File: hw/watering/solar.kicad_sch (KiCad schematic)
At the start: 23 parts, among them U2 DRV8220DSG, U5 STI3508

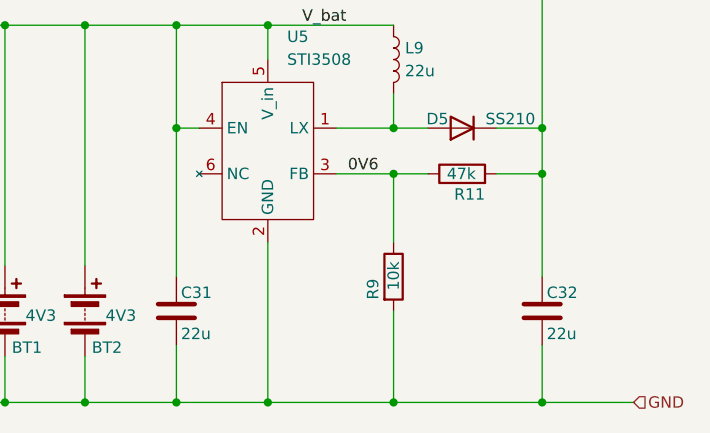
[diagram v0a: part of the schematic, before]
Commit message: - improved voltage boost on battery power - some issues with rtc clock - some issues with pwm that result in brownout
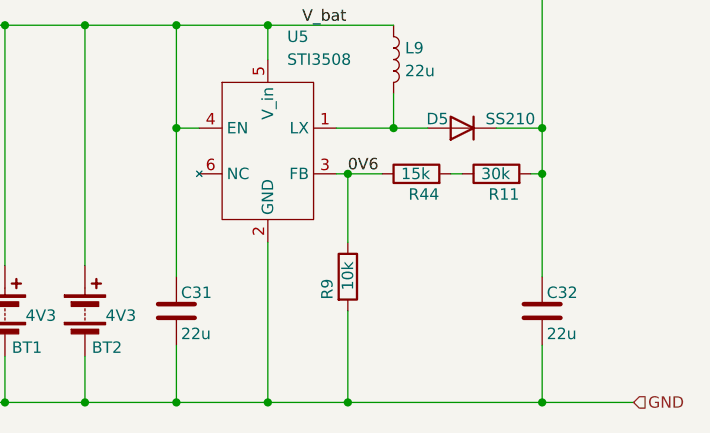
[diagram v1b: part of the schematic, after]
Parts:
- added R44: 15k, Resistor_SMD:R_0603_1608Metric, symbol Device:R
- R11: value 47k -> 30k
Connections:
- net 0V6: now also R44.1; no longer R11.1
- new net: R11.1, R44.2
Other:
- moved on the sheet: R11, R9
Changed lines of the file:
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@@
 	)
 	(junction
+		(at 389.89 220.98)
+		(diameter 0)
+		(color 0 0 0 0)
+	)
+	(junction
 		(at 389.89 246.38)
 		(diameter 0)
@@
 	)
 	(junction
-		(at 389.89 220.98)
-		(diameter 0)
-		(color 0 0 0 0)
-	)
-	(junction
 		(at 389.89 22.86)
 		(diameter 0)
@@
 	)
 	(junction
-		(at 373.38 246.38)
+		(at 368.3 246.38)
 		(diameter 0)
 		(color 0 0 0 0)
@@
 	)
 	(junction
-		(at 373.38 220.98)
-		(diameter 0)
-		(color 0 0 0 0)
-	)
-	(junction
 		(at 271.78 246.38)
 		(diameter 0)
@@
 	)
 	(junction
+		(at 368.3 220.98)
+		(diameter 0)
+		(color 0 0 0 0)
+	)
+	(junction
 		(at 349.25 204.47)
 		(diameter 0)
@@
 	(wire
 		(pts
-			(xy 349.25 246.38) (xy 373.38 246.38)
-		)
-		(stroke
-			(width 0)
-			(type default)
-		)
-	)
-	(wire
-		(pts
-			(xy 373.38 246.38) (xy 400.05 246.38)
+			(xy 349.25 246.38) (xy 368.3 246.38)
 		)
 		(stroke
@@
 	(wire
 		(pts
-			(xy 373.38 220.98) (xy 377.19 220.98)
+			(xy 77.47 227.33) (xy 77.47 217.17)
 		)
 		(stroke
@@
 	(wire
 		(pts
-			(xy 77.47 227.33) (xy 77.47 217.17)
+			(xy 86.36 223.52) (xy 86.36 217.17)
 		)
 		(stroke
@@
 	(wire
 		(pts
-			(xy 86.36 223.52) (xy 86.36 217.17)
+			(xy 236.22 208.28) (xy 252.73 208.28)
 		)
 		(stroke
@@
 	(wire
 		(pts
-			(xy 236.22 208.28) (xy 252.73 208.28)
+			(xy 309.88 246.38) (xy 313.69 246.38)
 		)
 		(stroke
@@
 	(wire
 		(pts
-			(xy 309.88 246.38) (xy 313.69 246.38)
+			(xy 388.62 220.98) (xy 389.89 220.98)
+		)
+		(stroke
+			(width 0)
+			(type default)
+		)
+	)
+	(wire
+		(pts
+			(xy 368.3 220.98) (xy 372.11 220.98)
 		)
 		(stroke
@@
 	(wire
 		(pts
-			(xy 367.03 220.98) (xy 373.38 220.98)
+			(xy 367.03 220.98) (xy 368.3 220.98)
 		)
 		(stroke
@@
 	(wire
 		(pts
-			(xy 373.38 220.98) (xy 373.38 228.6)
+			(xy 368.3 220.98) (xy 368.3 228.6)
 		)
 		(stroke
@@
 	(wire
 		(pts
-			(xy 373.38 236.22) (xy 373.38 246.38)
+			(xy 368.3 236.22) (xy 368.3 246.38)
 		)
 		(stroke
@@
 	(wire
 		(pts
-			(xy 384.81 220.98) (xy 389.89 220.98)
-		)
-		(stroke
-			(width 0)
-			(type default)
-		)
-	)
-	(wire
-		(pts
 			(xy 349.25 204.47) (xy 359.41 204.47)
 		)
@@
 	(wire
 		(pts
+			(xy 379.73 220.98) (xy 381 220.98)
+		)
+		(stroke
+			(width 0)
+			(type default)
+		)
+	)
+	(wire
+		(pts
 			(xy 86.36 242.57) (xy 86.36 246.38)
 		)
@@
 	(wire
 		(pts
+			(xy 368.3 246.38) (xy 400.05 246.38)
+		)
+		(stroke
+			(width 0)
+			(type default)
+		)
+	)
+	(wire
+		(pts
 			(xy 330.2 204.47) (xy 330.2 231.14)
 		)
@@
 	(symbol
 		(lib_id "Device:R")
-		(at 373.38 232.41 0)
+		(at 368.3 232.41 0)
 		(unit 1)
 		(body_style 1)
@@
 		(dnp no)
 		(property "Reference" "R9"
-			(at 371.094 234.95 90)
+			(at 366.014 234.95 90)
 			(show_name no)
 			(do_not_autoplace no)
@@
 		)
 		(property "Value" "10k"
-			(at 373.38 233.934 90)
+			(at 368.3 233.934 90)
 			(show_name no)
 			(do_not_autoplace no)
@@
 		)
 		(property "Footprint" "Resistor_SMD:R_0603_1608Metric"
-			(at 371.602 232.41 90)
+			(at 366.522 232.41 90)
 			(hide yes)
 			(show_name no)
@@
 		)
 		(property "Datasheet" "https://jlc-prod-smt.oss-eu-central-1.aliyuncs.com/smtDataManualFile/8579706381316128768-C25804.pdf?response-content-disposition=attachment%3B%20filename%3DC25804.pdf%3B%20filename%2A%3DUTF-8%27%27C25804.pdf&x-oss-date=20260604T182440Z&x-oss-expires=1800&x-oss-security-token=CAISgAN1q6Ft5B2yfSjIr5nhDvTiu55L8aayRHLFsEERZtthpKj%2B0Dz2IHhMdHJsAOodtv0%2FmmhT6PkclqRLcbhpcmfjV%2BZHzLB8qeRniENA4J7b16cNrbH4M4H6aXeirtuwDsz9SNTCALjPD3nPii50x5bjaDymRCbLGJaViJlhHLN1Ow6jdmhpCctxLAlvo9NgFxm3D%2Fu2NQPwiWf9FVdhvhEG6Vly8qOi2MaRmFy8yFTx0b0SvJ%2BjYMrmPctoN9JnSdC5mfdzau3a1TJ84gRD0a5wkaVA1zbDs5bfISEIuUzebreLqY03dV4mOvdqIcMe8qigz88fk%2FfIioH6xyxKOexoSCnFTOiiupCcQLPyao9jLu6iayqViY7QaIOTqQohZmkAMwVOasAsI3Ngh4zF97Qt0cVNkXO9gWfLI8DtuMleWhri1Udu3tHD0eS19jklBdzSlusJRAJJUVBflCeKEaRNSAd3WGhEfM2%2BBt4QT30w5N2u00S8OSMIOONBvqKWD5sagAGpldF62iBeHzrNV%2BHnUyjaA64BCjacRbVbSjmxSgiuNX1d%2FbCnqQV25prdqNhtDbAKCoRnNQDFNxmhLIIUUcffM9eG3oRc44RNhyi7hADN6z1ILjt6TEoRuXkDAYH1u8iyrE2YQDMkq7F3Cke8dxQ44PYZqWefci6GHDzQ1pzPpiAA&x-oss-signature-version=OSS4-HMAC-SHA256&x-oss-credential=STS.NZTENVVAjFdYFTtTADjTMKmU2%2F20260604%2Feu-central-1%2Foss%2Faliyun_v4_request&x-oss-signature=78c2b620008555fdaf271c3d0b7682edd0aca7d23428d31f63338848e1713cab"
-			(at 373.38 232.41 0)
+			(at 368.3 232.41 0)
 			(hide yes)
 			(show_name no)
@@
 		)
 		(property "Description" "C25804"
-			(at 373.38 232.41 0)
+			(at 368.3 232.41 0)
 			(hide yes)
 			(show_name no)
@@
 	)
 	(symbol
+		(lib_id "Device:R")
+		(at 375.92 220.98 90)
+		(unit 1)
+		(body_style 1)
+		(exclude_from_sim no)
+		(in_bom yes)
+		(on_board yes)
+		(in_pos_files yes)
+		(dnp no)
+		(property "Reference" "R44"
+			(at 378.46 223.266 90)
+			(show_name no)
+			(do_not_autoplace no)
+			(effects
+				(font
+					(size 1.27 1.27)
+				)
+				(justify left)
+			)
+		)
+		(property "Value" "15k"
+			(at 377.444 220.98 90)
+			(show_name no)
+			(do_not_autoplace no)
+			(effects
+				(font
+					(size 1.27 1.27)
+				)
+				(justify left)
+			)
+		)
+		(property "Footprint" "Resistor_SMD:R_0603_1608Metric"
+			(at 375.92 222.758 90)
+			(hide yes)
+			(show_name no)
+			(do_not_autoplace no)
+			(effects
+				(font
+					(size 1.27 1.27)
+				)
+			)
+		)
+		(property "Datasheet" "https://jlc-prod-smt.oss-eu-central-1.aliyuncs.com/smtDataManualFile/8579706364622934016-C25819.pdf?response-content-disposition=attachment%3B%20filename%3DC25819.pdf%3B%20filename%2A%3DUTF-8%27%27C25819.pdf&x-oss-date=20260604T212703Z&x-oss-expires=1800&x-oss-security-token=CAISgAN1q6Ft5B2yfSjIr5qGBvnBmah58ZCnSW2IvnU%2FOOZNta3duzz2IHhMdHJsAOodtv0%2FmmhT6PkclqRLcbhpcmfjV%2BZHzLB8qc9%2FokVA4J7b16cNrbH4M4H6aXeirtuwDsz9SNTCALjPD3nPii50x5bjaDymRCbLGJaViJlhHLN1Ow6jdmhpCctxLAlvo9NgFxm3D%2Fu2NQPwiWf9FVdhvhEG6Vly8qOi2MaRmFy8yFTx0b0SvJ%2BjYMrmPctoN9JnSdC5mfdzau3a1TJ84gRD0a5wkaVA1zbDs5bfISEIuUzebreLqY03dV4mOvdqIcMe8qigz88fk%2FfIioH6xyxKOexoSCnFTOiiupCcQLPyao9jLu6iayqViY7QaIOTqQohZmkAMwVOasAsI3Ngh4zF97Qt0cVNkXO9gWfLI8DtuMleWqrvQN5iAnSgc5lCkRRYwGs1287ugXlSQzo890KPDAEovaKCnZ2ZSfh7Y4sNknI6i%2Bfc2Se2MIkILjrImKKWD5sagAFp6e2CTF5gXCAetl%2FZznzBeiqXvbdtrNp24XwBckBwOk4pCo9PLwSFMgOtQSf5U6kP%2F%2Bd1fI%2BKr022AwW2hsiCSfA6ItkAjrYqmnkpM1k6ce1E8ls7kKfeT%2Fq%2FikPDk77ij56kdNpXvKHTlexuI%2FHtV9DEGaEJEWVb894cTL2j2iAA&x-oss-signature-version=OSS4-HMAC-SHA256&x-oss-credential=STS.NY3MCutwXFRLKK9Zuj4iaZhvY%2F20260604%2Feu-central-1%2Foss%2Faliyun_v4_request&x-oss-signature=39443662dce0733909bc9974c7f7cc05e9a3997f7aeb5536bfa6dcd917da7abb"
+			(at 375.92 220.98 0)
+			(hide yes)
+			(show_name no)
+			(do_not_autoplace no)
+			(effects
+				(font
+					(size 1.27 1.27)
+				)
+			)
+		)
+		(property "Description" "C22809"
+			(at 375.92 220.98 0)
+			(hide yes)
+			(show_name no)
+			(do_not_autoplace no)
+			(effects
+				(font
+					(size 1.27 1.27)
+				)
+			)
+		)
+		(pin "1"
+		)
+		(pin "2"
+		)
+		(instances
+			(project "watering"
+				(path "/cfeeaa6f-be25-403f-b03c-39be367d5a74/dc41958e-1f08-40e2-b7ec-874562e0f9ea"
+					(reference "R44")
+					(unit 1)
+				)
+			)
+		)
+	)
+	(symbol
 		(lib_id "Device:D")
 		(at 381 215.9 180)
@@
 	(symbol
 		(lib_id "Device:R")
-		(at 381 220.98 90)
+		(at 384.81 220.98 90)
 		(unit 1)
 		(body_style 1)
@@
 		(dnp no)
 		(property "Reference" "R11"
-			(at 383.54 223.266 90)
+			(at 387.35 223.266 90)
 			(show_name no)
 			(do_not_autoplace no)
@@
 			)
 		)
-		(property "Value" "47k"
-			(at 382.524 220.98 90)
+		(property "Value" "30k"
+			(at 386.334 220.98 90)
 			(show_name no)
 			(do_not_autoplace no)
@@
 		)
 		(property "Footprint" "Resistor_SMD:R_0603_1608Metric"
-			(at 381 222.758 90)
+			(at 384.81 222.758 90)
 			(hide yes)
 			(show_name no)
@@
 		)
 		(property "Datasheet" "https://jlc-prod-smt.oss-eu-central-1.aliyuncs.com/smtDataManualFile/8579706364622934016-C25819.pdf?response-content-disposition=attachment%3B%20filename%3DC25819.pdf%3B%20filename%2A%3DUTF-8%27%27C25819.pdf&x-oss-date=20260604T212703Z&x-oss-expires=1800&x-oss-security-token=CAISgAN1q6Ft5B2yfSjIr5qGBvnBmah58ZCnSW2IvnU%2FOOZNta3duzz2IHhMdHJsAOodtv0%2FmmhT6PkclqRLcbhpcmfjV%2BZHzLB8qc9%2FokVA4J7b16cNrbH4M4H6aXeirtuwDsz9SNTCALjPD3nPii50x5bjaDymRCbLGJaViJlhHLN1Ow6jdmhpCctxLAlvo9NgFxm3D%2Fu2NQPwiWf9FVdhvhEG6Vly8qOi2MaRmFy8yFTx0b0SvJ%2BjYMrmPctoN9JnSdC5mfdzau3a1TJ84gRD0a5wkaVA1zbDs5bfISEIuUzebreLqY03dV4mOvdqIcMe8qigz88fk%2FfIioH6xyxKOexoSCnFTOiiupCcQLPyao9jLu6iayqViY7QaIOTqQohZmkAMwVOasAsI3Ngh4zF97Qt0cVNkXO9gWfLI8DtuMleWqrvQN5iAnSgc5lCkRRYwGs1287ugXlSQzo890KPDAEovaKCnZ2ZSfh7Y4sNknI6i%2Bfc2Se2MIkILjrImKKWD5sagAFp6e2CTF5gXCAetl%2FZznzBeiqXvbdtrNp24XwBckBwOk4pCo9PLwSFMgOtQSf5U6kP%2F%2Bd1fI%2BKr022AwW2hsiCSfA6ItkAjrYqmnkpM1k6ce1E8ls7kKfeT%2Fq%2FikPDk77ij56kdNpXvKHTlexuI%2FHtV9DEGaEJEWVb894cTL2j2iAA&x-oss-signature-version=OSS4-HMAC-SHA256&x-oss-credential=STS.NY3MCutwXFRLKK9Zuj4iaZhvY%2F20260604%2Feu-central-1%2Foss%2Faliyun_v4_request&x-oss-signature=39443662dce0733909bc9974c7f7cc05e9a3997f7aeb5536bfa6dcd917da7abb"
-			(at 381 220.98 0)
+			(at 384.81 220.98 0)
 			(hide yes)
 			(show_name no)
@@
 			)
 		)
-		(property "Description" "C25819"
-			(at 381 220.98 0)
+		(property "Description" "C22984"
+			(at 384.81 220.98 0)
 			(hide yes)
 			(show_name no)
